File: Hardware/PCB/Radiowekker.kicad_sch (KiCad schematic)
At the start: 2 parts

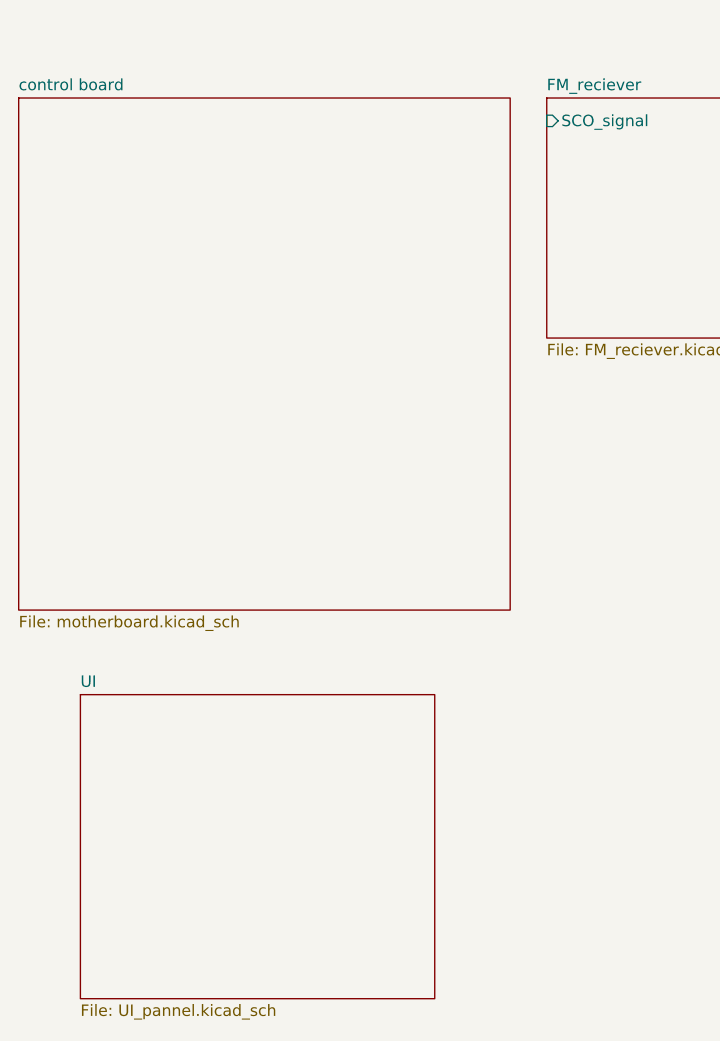
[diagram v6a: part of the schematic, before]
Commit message: added connection hierachie pins
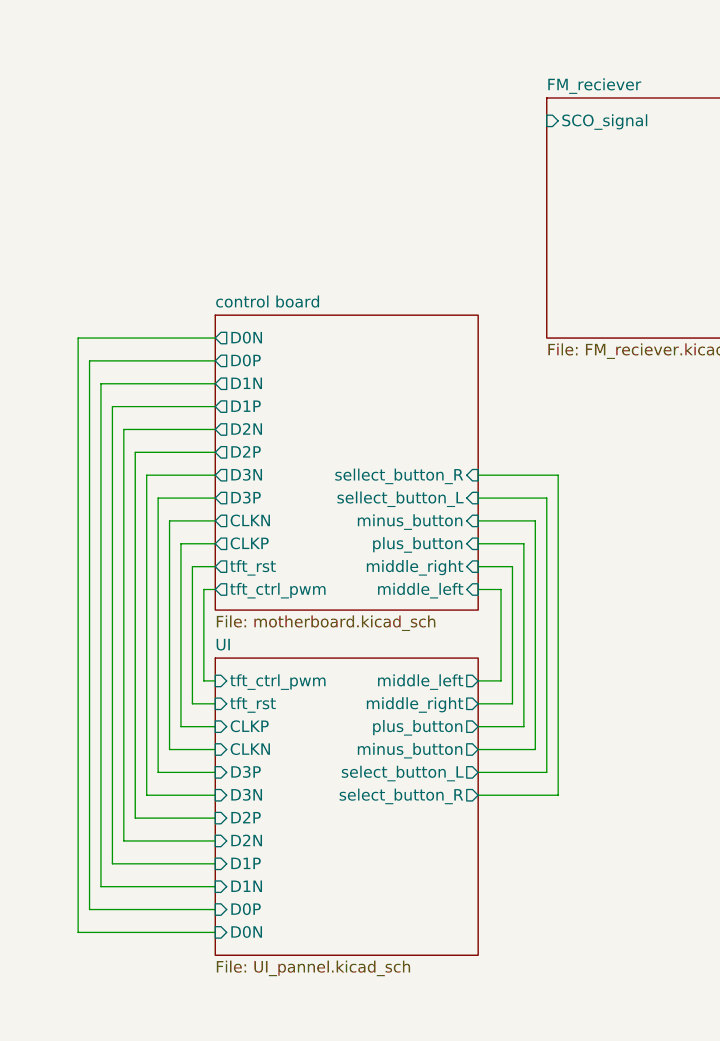
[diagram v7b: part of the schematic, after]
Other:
- sheet UI ports: added CLKN, CLKP, D0N, D0P, D1N, D1P, D2N, D2P, D3N, D3P, middle_left, middle_right, minus_button, plus_button, select_button_L, select_button_R, tft_ctrl_pwm, tft_rst; removed none
- sheet control board ports: added CLKN, CLKP, D0N, D0P, D1N, D1P, D2N, D2P, D3N, D3P, middle_left, middle_right, minus_button, plus_button, sellect_button_L, sellect_button_R, tft_ctrl_pwm, tft_rst; removed none

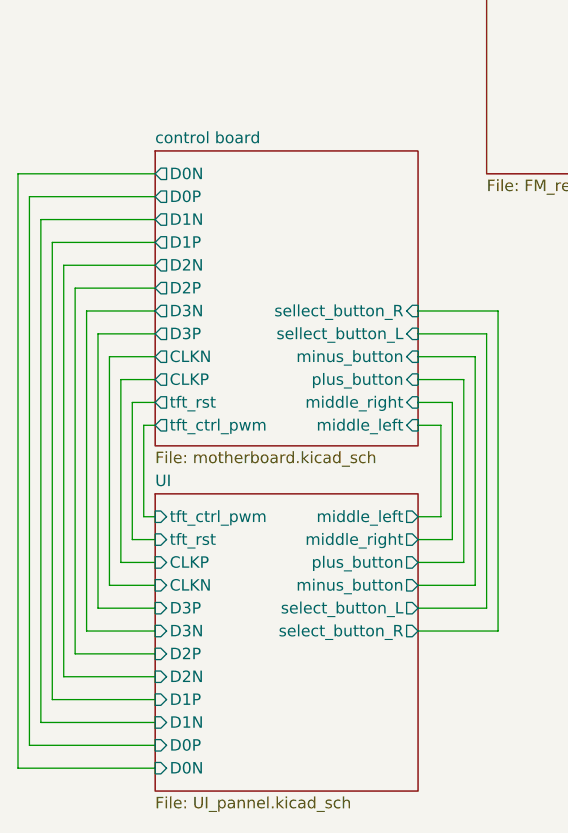
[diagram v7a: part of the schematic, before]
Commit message: added new screen and updated mcu to a more compatible one
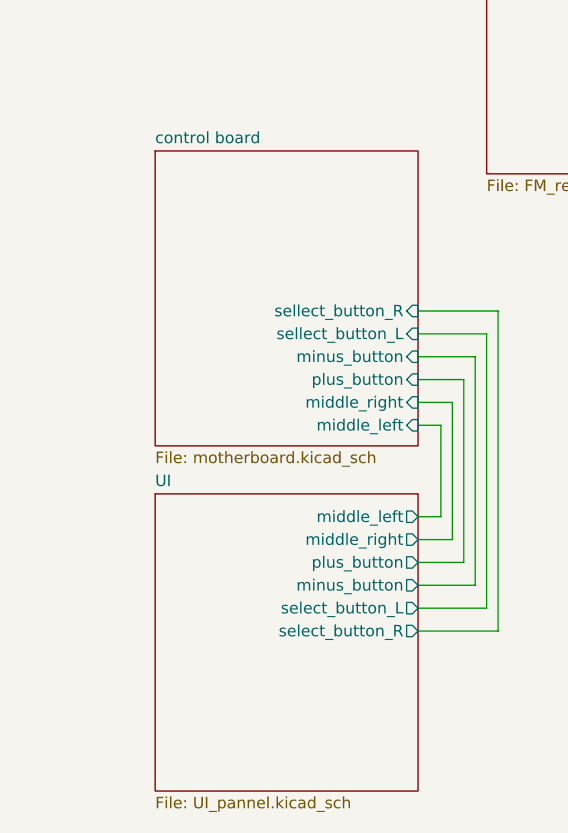
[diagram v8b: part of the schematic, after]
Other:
- sheet UI ports: added none; removed CLKN, CLKP, D0N, D0P, D1N, D1P, D2N, D2P, D3N, D3P, tft_ctrl_pwm, tft_rst
- sheet control board ports: added none; removed CLKN, CLKP, D0N, D0P, D1N, D1P, D2N, D2P, D3N, D3P, tft_ctrl_pwm, tft_rst
